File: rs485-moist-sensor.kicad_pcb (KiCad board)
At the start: 4 copper layers, 18 x 149 mm, 33 parts, among them IC1 ATTINY441-SSU, P1 CONN_02X03, P2 CONN_01X04, Q1 Q_PMOS_GSD, U1 SN65HVD72, U2 MCP1702, X1 16MHz

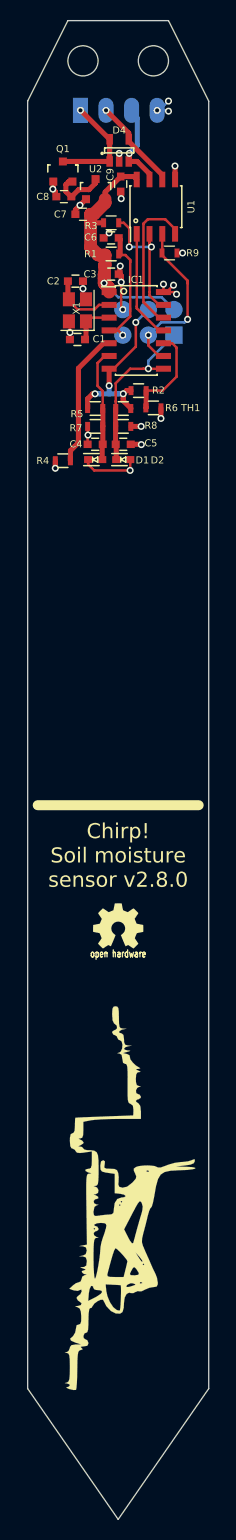
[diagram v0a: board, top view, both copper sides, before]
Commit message: Update the sensor outline to accomodate narrower heatshrink. Also change ziptie application feature
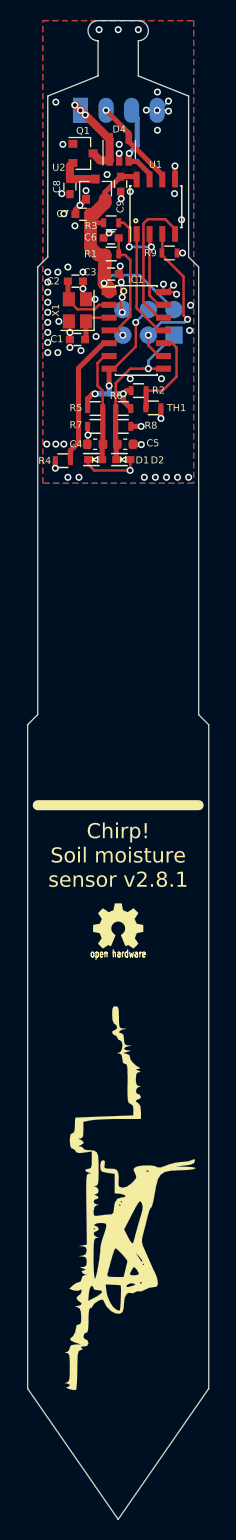
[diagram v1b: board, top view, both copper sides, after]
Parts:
- removed MK1, MK2: Mounting_Hole, Mounting_Holes:MountingHole_3mm
- C4, C5: footprint Capacitors_SMD:C_0603 -> Capacitor_SMD:C_0603_1608Metric
- D4: footprint Housings_SOT-23_SOT-143_TSOT-6:SOT-23-5 -> Package_TO_SOT_SMD:SOT-23-5
- Q1, U2: footprint Housings_SOT-23_SOT-143_TSOT-6:SOT-23 -> Package_TO_SOT_SMD:SOT-23
- moved Q1 2.69 mm to (91.5, 26.2)
- moved C8 1.17 mm to (90.2, 29.5), turned to -90 degrees
- moved C5 0.20 mm to (95.7, 55.1)
- moved D4 0.10 mm to (95.1, 25.8)
- turned U2 to 90 degrees
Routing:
- net VCC: track 10.9 -> 9.00 mm, vias 1 -> 3
- net GND: track 27.8 -> 26.2 mm, vias 22 -> 71
- net Net-(C8-Pad1): track 5.59 -> 4.27 mm
- net +3V3: track 25.2 -> 25.9 mm
- added copper zone on B.Cu, net GND
- added copper zone on F.Cu, net GND
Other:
- outline, holes or cut-outs redrawn
- board text added: "Chirp! Soil moisture sensor v2.8.1"
- board text removed: "Chirp! Soil moisture sensor v2.8.0"

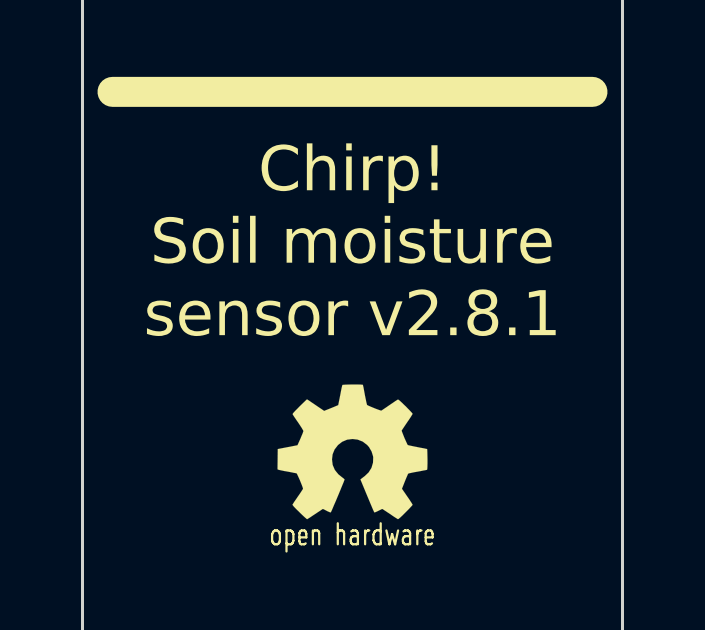
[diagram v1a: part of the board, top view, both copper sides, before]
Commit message: Update capacitance to accomodate crystal change. Tidyup fabrication layers
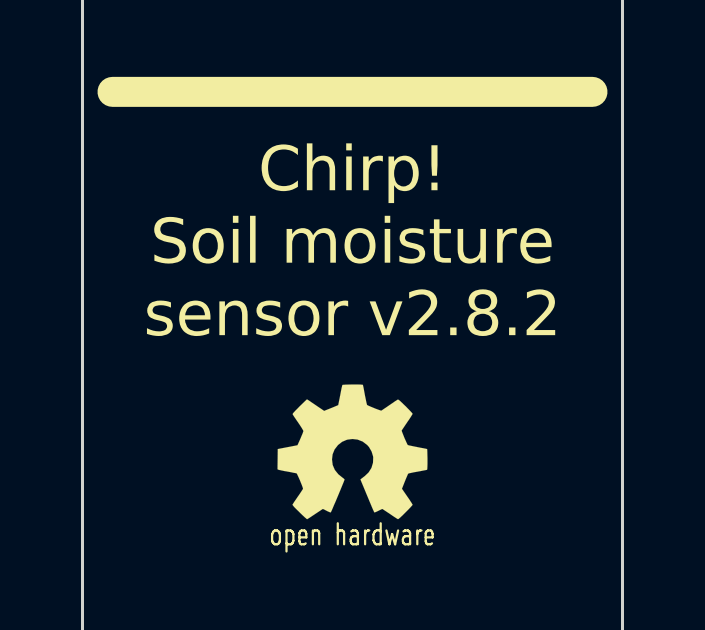
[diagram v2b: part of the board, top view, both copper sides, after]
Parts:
- C1, C2: value 33p -> 13p
- D1, D2: value BAT54 -> RB751S40
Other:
- board text added: "Chirp! Soil moisture sensor v2.8.2"
- board text removed: "Chirp! Soil moisture sensor v2.8.1"
